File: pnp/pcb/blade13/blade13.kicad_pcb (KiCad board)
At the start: 2 copper layers, 200.6 x 26.6 mm, 54 parts, among them J1 IN, J10 SPRING_PINS, J11 SPRING_PINS, J12 SPRING_PINS, J13 SPRING_PINS, J14 SPRING_PINS, J15 SPRING_PINS, J2 OUT, J3 SPRING_PINS, J4 SPRING_PINS, J5 SPRING_PINS, J6 SPRING_PINS, J7 SPRING_PINS, J8 SPRING_PINS, J9 SPRING_PINS, U1 DS28E07, U10 DS28E07, U11 DS28E07, U12 DS28E07, U13 DS28E07, U2 DS28E07, U3 DS28E07, U4 DS28E07, U5 DS28E07, U6 DS28E07, U7 DS28E07, U8 DS28E07, U9 DS28E07

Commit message: updates blades
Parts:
- moved kibuzzard-65FDDA59 10.2 mm to (112.2, 60.1)
- moved kibuzzard-65FDDA61 0.81 mm to (112.0, 55.2)

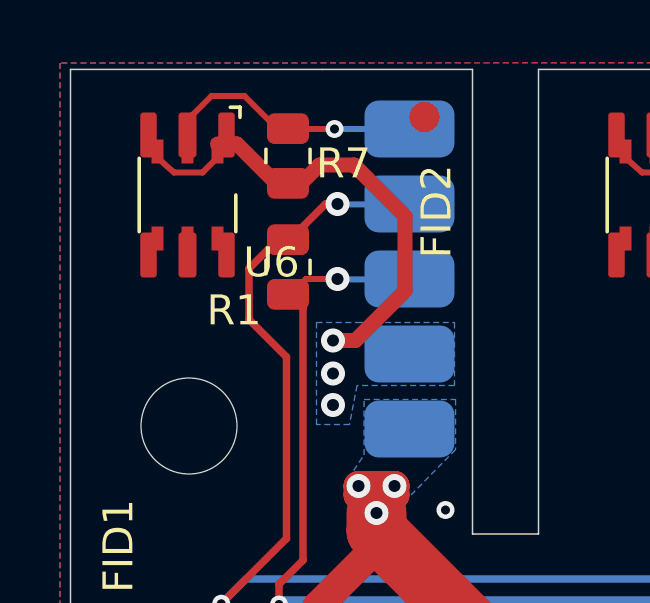
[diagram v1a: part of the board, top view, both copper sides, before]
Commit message: adds copper keepout to blade countersink holes
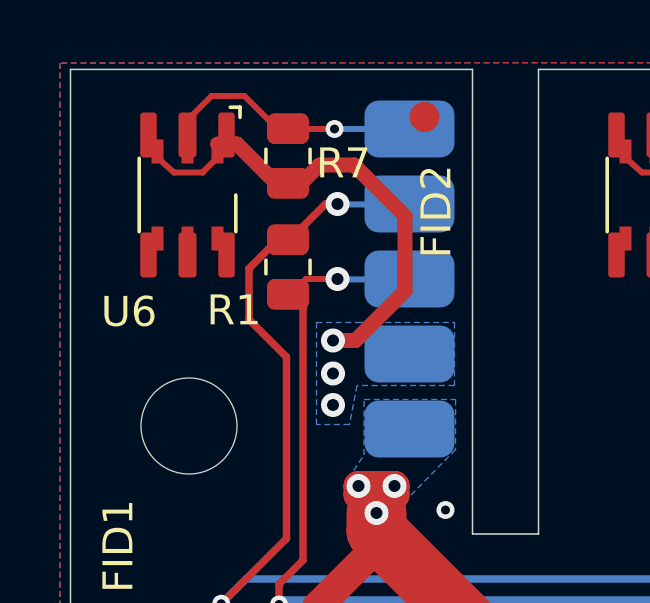
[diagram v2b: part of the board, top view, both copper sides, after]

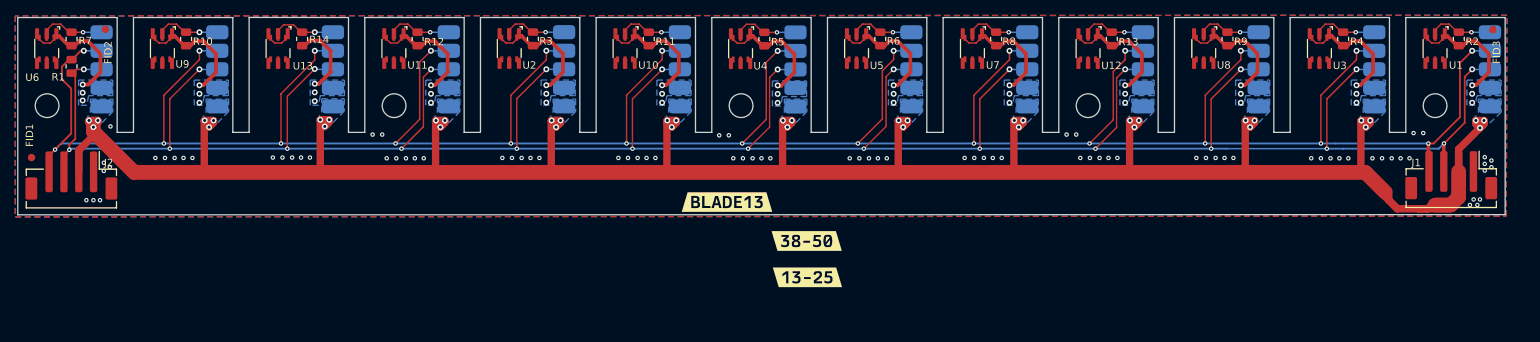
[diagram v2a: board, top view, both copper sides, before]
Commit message: adds slightly larger spaced blade pcb, plus a slightly increased 13 blade print. still needs 12
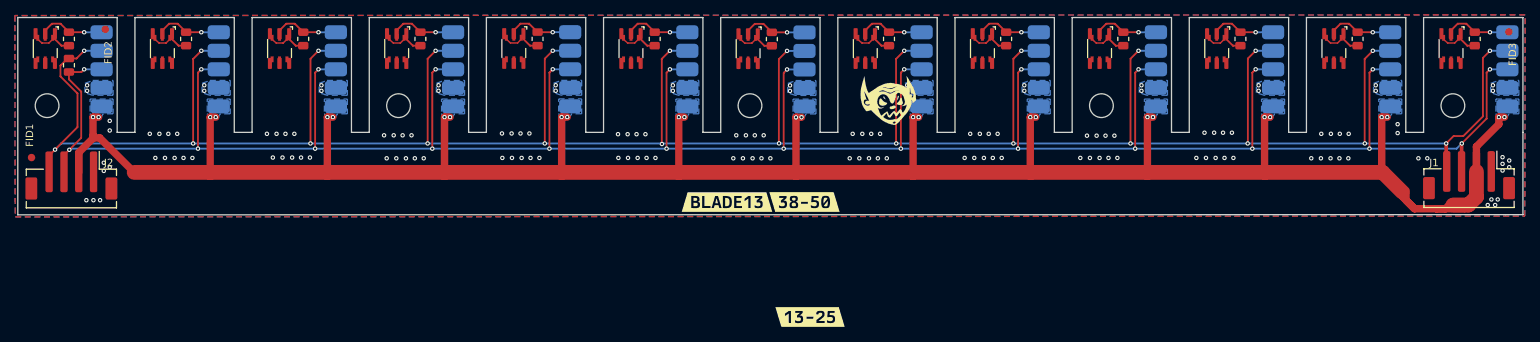
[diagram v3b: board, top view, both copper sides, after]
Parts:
- moved kibuzzard-65FDDA59 5.36 mm to (112.5, 65.5)
- moved kibuzzard-65FDDA61 5.26 mm to (111.8, 50.0)
- moved G*** 4.20 mm to (123.1, 36.8), turned to 5 degrees
- moved J1 2.40 mm to (201.4, 46.4)
- moved H5 2.40 mm to (199.2, 37.0)
- moved J3 2.35 mm to (206.6, 27.1)
- moved FID3 2.17 mm to (206.8, 27.1)
- moved U1 2.15 mm to (199.0, 29.3)
- moved R2 2.15 mm to (202.2, 28.0)
- moved J5 2.15 mm to (190.7, 27.1)
- moved U3 1.95 mm to (183.2, 29.3)
- moved R4 1.95 mm to (186.3, 28.0)
- moved J10 1.95 mm to (174.9, 27.1)
- moved H4 1.80 mm to (151.8, 37.0)
- moved R9 1.75 mm to (170.6, 28.0)
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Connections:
- J1 pad MP: (no net) -> GND
- J2 pad MP: (no net) -> GND
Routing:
- net GND: track 169.2 -> 35.6 mm, vias 123 -> 146
- net VIN: track 343.4 -> 310.7 mm, vias 39 -> 26
- net RS-485+: track 414.5 -> 401.5 mm
- net RS-485-: track 383.8 -> 371.1 mm
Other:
- board size 200.6 x 26.6 mm -> 203 x 26.6 mm
